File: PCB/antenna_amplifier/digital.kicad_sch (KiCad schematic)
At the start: 26 parts, among them J401 AES3 OUT, SW401 CS8406 MODE, U401 CS8406, Y401 24.576MHz, Y402 24.576MHz

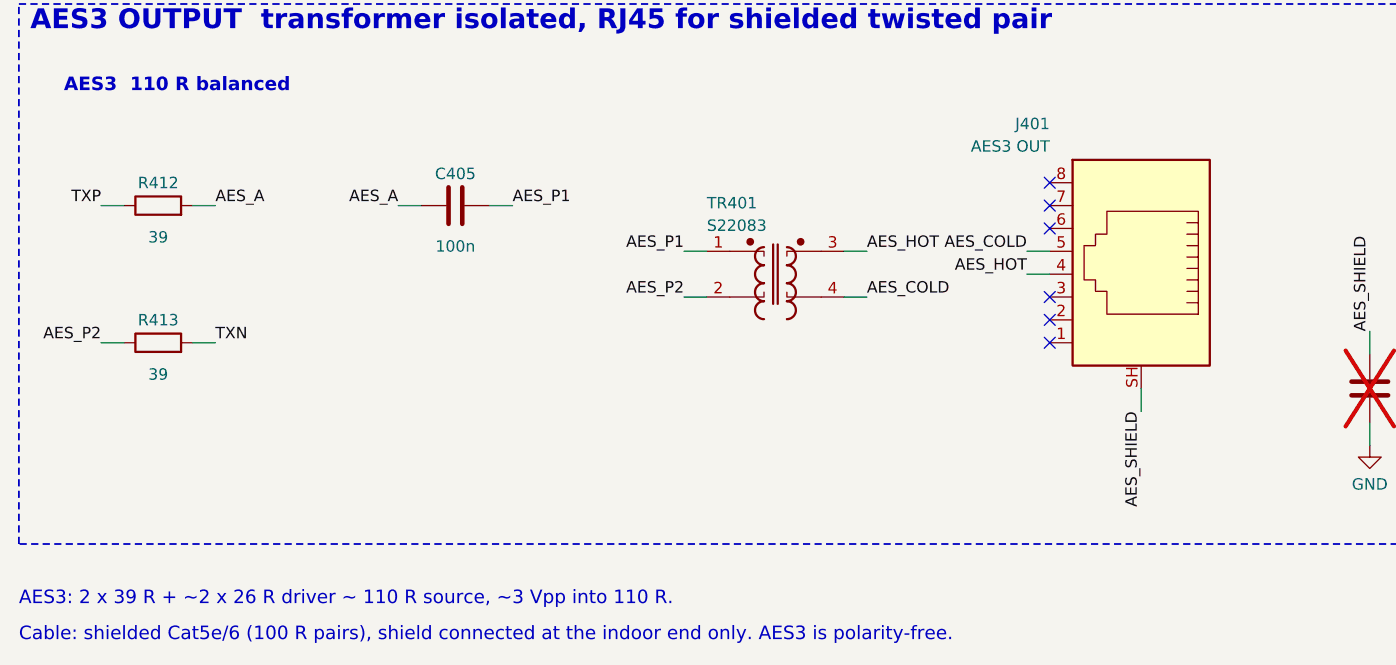
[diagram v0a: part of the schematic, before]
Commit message: AES3 source resistors 22 ohm for a 111 ohm source; tidy schematics and assembly drawings
- R412/R413 2 x 39 -> 2 x 22 ohm (Vishay TNPW060322R0BEEA, anti-sulfur): the
  CS8406 drivers are 33.5 ohm each at VL = 3.3 V, so 2 x 39 gave a 145 ohm
  source, outside AES3's 110 ohm +-20 %. The schematic note had used the 5 V
  figure and mis-added it.
- AES3 sheet: transformer flipped (kicadgen gains mirror='x') and wired straight
  to R412/R413/C405 and the RJ45, no more touching AES_HOT/AES_COLD labels.
- Stale S/PDIF and 9 V wording out of the sheets and BOM: DC input block reads
  6.98-15 V, J101 'DC IN', PSU J2 'DC OUT', reset button and clock branch say
  AES3; the legacy +9V / +9V_OUT net names are explained on the sheets.
- PSU root sheet gets the same power-path / board summary as the amplifier.
- Assembly drawings: fab-layer copies of the references removed wherever the
  silk reference shows (KiCad 9 texts cannot be hidden), so each part is named
  once; J201/J202 (no silk on the guard island) get theirs beside the part.
- BOM totals +0.14 EUR (502.15 ex VAT reference build, 407.22 recommended).

Co-Authored-By: Claude Opus 5.5 <noreply@anthropic.com>
Claude-Session: https://claude.ai/code/session_01RsM1DhHhY1tSr2aHjVygSC
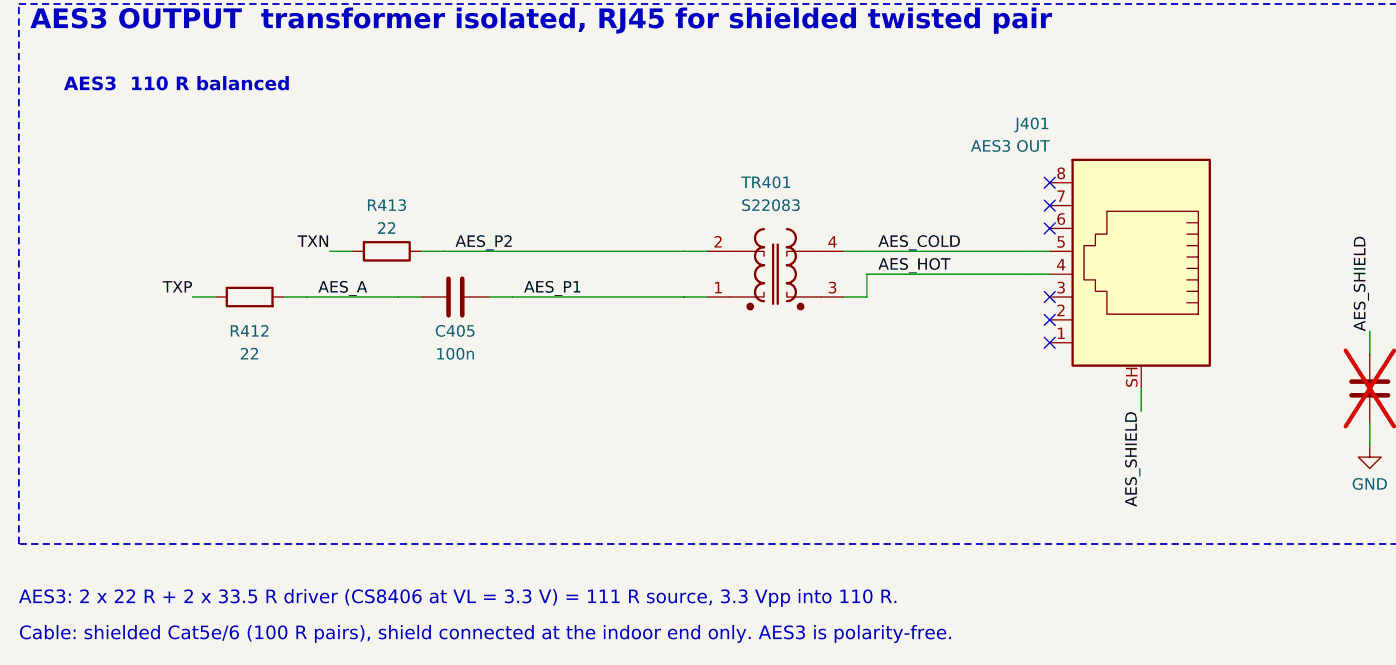
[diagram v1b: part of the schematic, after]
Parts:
- R402: Role series termination, S/PDIF branch -> series termination, AES3 TX branch
- R412, R413: value 39 -> 22; MPN ERA-3AEB390V -> TNPW060322R0BEEA; Manufacturer Panasonic -> Vishay Dale
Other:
- note added: "AES3: 2 x 22 R + 2 x 33.5 R driver (CS8406 at VL = 3.3 V) = 111 R source, 3.3 Vpp into 110 R."
- note removed: "AES3: 2 x 39 R + ~2 x 26 R driver ~ 110 R source, ~3 Vpp into 110 R."
- moved on the sheet: C405, R412, R413, TR401
